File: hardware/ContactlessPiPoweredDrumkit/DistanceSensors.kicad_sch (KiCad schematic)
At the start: 0 parts

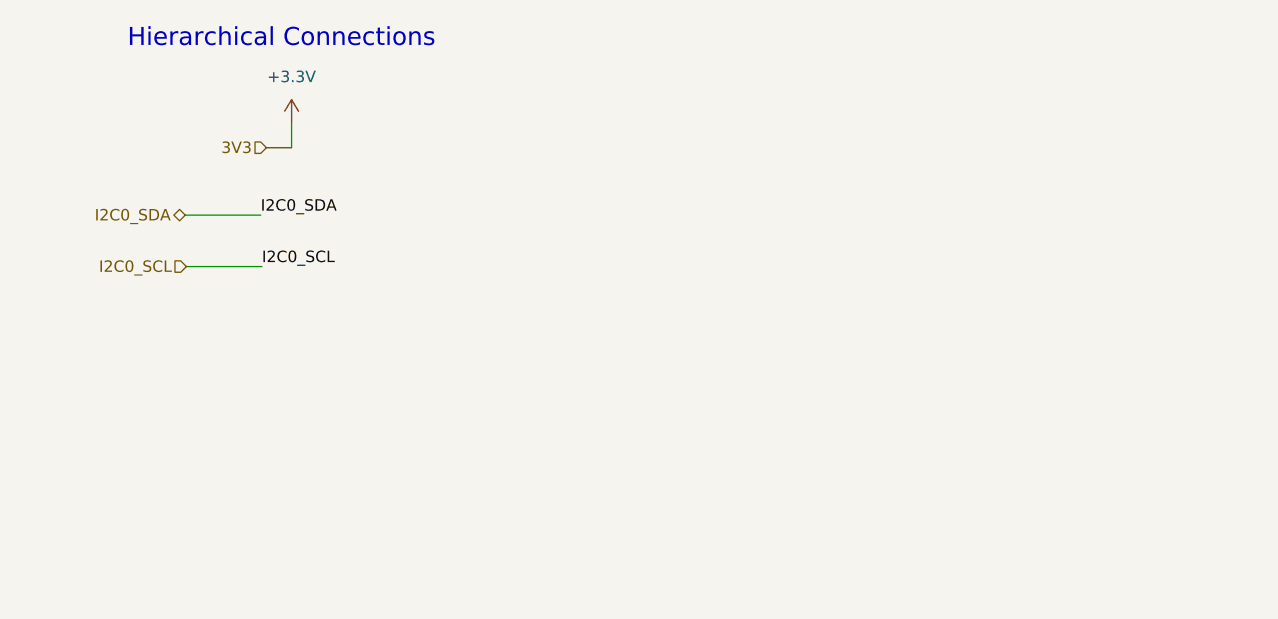
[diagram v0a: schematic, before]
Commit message: Add Hierarchical Connections and Distance Sensors
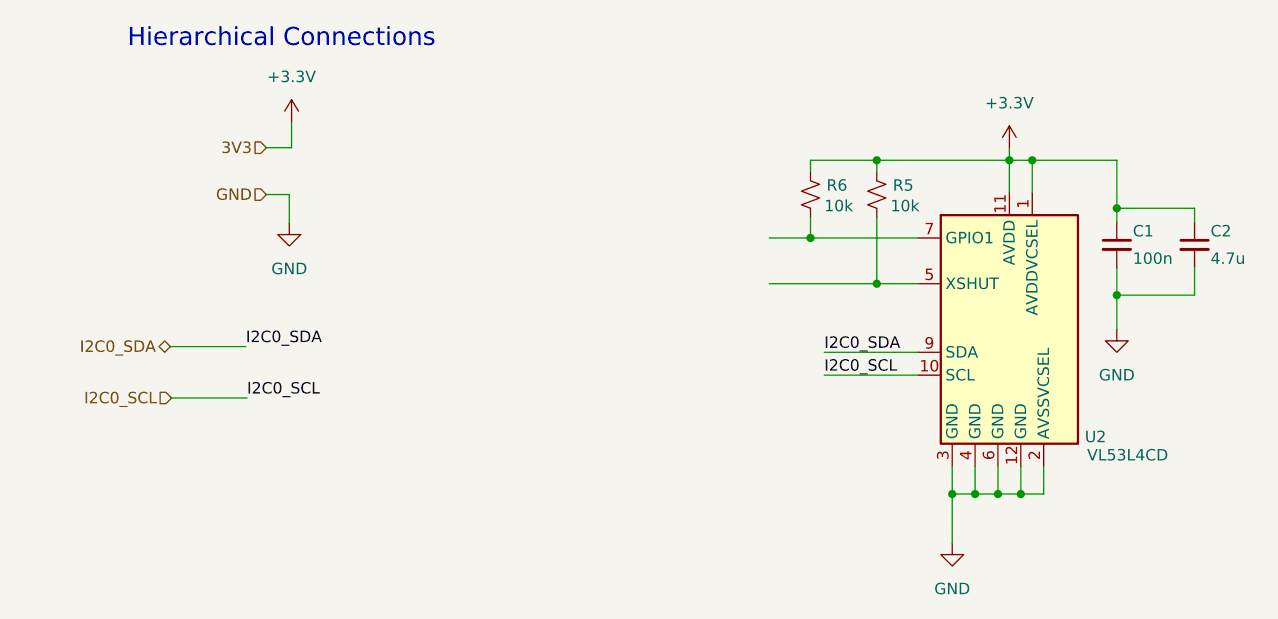
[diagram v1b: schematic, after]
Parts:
- added C1: 100n, symbol Device:C_Small
- added C2: 4.7u, symbol Device:C_Small
- added R5, R6: 10k, symbol Device:R_Small_US
- added U2: VL53L4CD, symbol ContactlessPPD_custom_lib:VL53L4CD
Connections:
- net +3.3V: now also C1.1, C2.1, R5.1, R6.1, U2.1 (AVDDVCSEL), U2.11 (AVDD)
- net I2C0_SCL: now also U2.10 (SCL)
- net I2C0_SDA: now also U2.9 (SDA)
- new net: R6.2, U2.7 (GPIO1)
- new net: R5.2, U2.5 (XSHUT)
- new net GND: C1.2, C2.2, U2.12 (GND), U2.2 (AVSSVCSEL), U2.3 (GND), U2.4 (GND), U2.6 (GND)
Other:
- title: (none) -> Distance Sensors
